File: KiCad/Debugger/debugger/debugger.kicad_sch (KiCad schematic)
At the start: 5 parts, among them J1 Conn_02x16_Odd_Even, J2 Conn_02x16_Odd_Even, J3 CPU Signals, J4 Conn_02x18_Odd_Even

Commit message: debugger wip
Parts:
- removed J1, J2: Conn_02x16_Odd_Even, Connector_PinHeader_2.54mm:PinHeader_2x16_P2.54mm_Vertical, symbol Connector_Generic:Conn_02x16_Odd_Even
- removed J3: CPU Signals, Connector_PinHeader_2.54mm:PinHeader_2x06_P2.54mm_Vertical, symbol 6502-computer-cache:Connector_Generic_Conn_02x06_Odd_Even
- added J10, J19, J7, J8, J9: Conn_01x08, Connector_PinSocket_2.54mm:PinSocket_1x08_P2.54mm_Vertical, symbol Connector_Generic:Conn_01x08
- added J11, J12, J13, J14, J18, J20, J3, J4, J5, J6: Conn_01x08, Connector_PinHeader_2.54mm:PinHeader_1x08_P2.54mm_Vertical, symbol Connector_Generic:Conn_01x08
- added J15, J17: Conn_01x10, Connector_PinHeader_2.54mm:PinHeader_1x10_P2.54mm_Vertical, symbol Connector_Generic:Conn_01x10
- added J16: Conn_01x10, Connector_PinSocket_2.54mm:PinSocket_1x10_P2.54mm_Vertical, symbol Connector_Generic:Conn_01x10
- added J2: Conn_02x20_Odd_Even, Connector_IDC:IDC-Header_2x20_P2.54mm_Vertical, symbol Connector_Generic:Conn_02x20_Odd_Even
- added J21: Conn_02x18_Odd_Even, Connector_PinHeader_2.54mm:PinHeader_2x18_P2.54mm_Vertical, symbol Connector_Generic:Conn_02x18_Odd_Even
- renumbered J4 to J1
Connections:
- net GND: now also J2.34 (Pin_34), J2.35 (Pin_35), J21.35 (Pin_35), J21.36 (Pin_36)
- net RDY: now also J1.4 (Pin_4), XA1.D23, J2.2 (Pin_2), J21.4 (Pin_4); no longer J1.3 (Pin_3)
- net R~{W}: now also J1.7 (Pin_7), XA1.D28, J2.7 (Pin_7), J21.7 (Pin_7); no longer J1.8 (Pin_8)
- net SYNC: now also J1.10 (Pin_10), XA1.D29, J2.8 (Pin_8), J21.10 (Pin_10); no longer J1.9 (Pin_9)
- net a0: now also J1.12 (Pin_12), XA1.D31, J2.10 (Pin_10), J21.12 (Pin_12); no longer J1.11 (Pin_11)
- net a1: now also J1.14 (Pin_14), XA1.D33, J2.12 (Pin_12), J21.14 (Pin_14); no longer J1.13 (Pin_13)
- net a10: now also J1.32 (Pin_32), XA1.D51 (D51_MOSI), J2.30 (Pin_30), J21.32 (Pin_32); no longer J1.31 (Pin_31)
- net a11: now also J1.34 (Pin_34), XA1.D53 (D53_CS), J2.32 (Pin_32), J21.34 (Pin_34); no longer J1.33 (Pin_33)
- net a12: now also J1.33 (Pin_33), XA1.D52 (D52_SCK), J2.33 (Pin_33), J21.33 (Pin_33); no longer J1.34 (Pin_34)
- net a13: now also J1.31 (Pin_31), XA1.D50 (D50_MISO), J2.31 (Pin_31), J21.31 (Pin_31); no longer J1.32 (Pin_32)
- net a14: now also J1.29 (Pin_29), XA1.D48, J2.29 (Pin_29), J21.29 (Pin_29); no longer J1.30 (Pin_30)
- net a15: now also J1.27 (Pin_27), XA1.D46, J2.27 (Pin_27), J21.27 (Pin_27); no longer J1.28 (Pin_28)
- net a2: now also J1.16 (Pin_16), XA1.D35, J2.14 (Pin_14), J21.16 (Pin_16); no longer J1.15 (Pin_15)
- net a3: now also J1.18 (Pin_18), XA1.D37, J2.16 (Pin_16), J21.18 (Pin_18); no longer J1.17 (Pin_17)
- net a4: now also J1.20 (Pin_20), XA1.D39, J2.18 (Pin_18), J21.20 (Pin_20); no longer J1.19 (Pin_19)
- net a5: now also J1.22 (Pin_22), XA1.D41, J2.20 (Pin_20), J21.22 (Pin_22); no longer J1.21 (Pin_21)
- net a6: now also J1.24 (Pin_24), XA1.D43, J2.22 (Pin_22), J21.24 (Pin_24); no longer J1.23 (Pin_23)
- net a7: now also J1.26 (Pin_26), XA1.D45, J2.24 (Pin_24), J21.26 (Pin_26); no longer J1.25 (Pin_25)
- net a8: now also J1.28 (Pin_28), XA1.D47, J2.26 (Pin_26), J21.28 (Pin_28); no longer J1.27 (Pin_27)
- net a9: now also J1.30 (Pin_30), XA1.D49, J2.28 (Pin_28), J21.30 (Pin_30); no longer J1.29 (Pin_29)
- net d0: now also J1.11 (Pin_11), XA1.D30, J2.11 (Pin_11), J21.11 (Pin_11); no longer J1.12 (Pin_12)
- net d1: now also J1.13 (Pin_13), XA1.D32, J2.13 (Pin_13), J21.13 (Pin_13); no longer J1.14 (Pin_14)
- net d2: now also J1.15 (Pin_15), XA1.D34, J2.15 (Pin_15), J21.15 (Pin_15); no longer J1.16 (Pin_16)
- net d3: now also J1.17 (Pin_17), XA1.D36, J2.17 (Pin_17), J21.17 (Pin_17); no longer J1.18 (Pin_18)
- net d4: now also J1.19 (Pin_19), XA1.D38, J2.19 (Pin_19), J21.19 (Pin_19); no longer J1.20 (Pin_20)
- net d5: now also J1.21 (Pin_21), XA1.D40, J2.21 (Pin_21), J21.21 (Pin_21); no longer J1.22 (Pin_22)
- net d6: now also J1.23 (Pin_23), XA1.D42, J2.23 (Pin_23), J21.23 (Pin_23); no longer J1.24 (Pin_24)
- net d7: now also J1.25 (Pin_25), XA1.D44, J2.25 (Pin_25), J21.25 (Pin_25); no longer J1.26 (Pin_26)
- net ~{BE}: now also J1.5 (Pin_5), XA1.D26, J2.5 (Pin_5), J21.5 (Pin_5); no longer J1.6 (Pin_6)
- net ~{IRQ}: now also J1.6 (Pin_6), XA1.D25, J2.4 (Pin_4), J21.6 (Pin_6); no longer J1.5 (Pin_5)
- net ~{NMI}: now also J1.8 (Pin_8), XA1.D27, J2.6 (Pin_6), J21.8 (Pin_8); no longer J1.7 (Pin_7)
- net ~{RES}: now also J1.1 (Pin_1), XA1.D22, J2.1 (Pin_1), J21.1 (Pin_1); no longer J1.2 (Pin_2)
- net ~{SO}: now also J1.3 (Pin_3), XA1.D24, J2.3 (Pin_3), J21.3 (Pin_3); no longer J1.4 (Pin_4)
- net at XA1.3V3 (3.3V): now also J18.5 (Pin_5), J19.5 (Pin_5), J20.4 (Pin_4)
- net at XA1.5V1 (5V): now also J18.4 (Pin_4), J19.4 (Pin_4), J20.5 (Pin_5)
- net at XA1.A0: now also J11.1 (Pin_1), J3.1 (Pin_1), J7.1 (Pin_1)
- net at XA1.A1: now also J11.2 (Pin_2), J3.2 (Pin_2), J7.2 (Pin_2)
- net at XA1.A10: now also J14.6 (Pin_6), J4.3 (Pin_3), J9.6 (Pin_6)
- net at XA1.A11: now also J14.5 (Pin_5), J4.4 (Pin_4), J9.5 (Pin_5)
- net at XA1.A12: now also J14.4 (Pin_4), J4.5 (Pin_5), J9.4 (Pin_4)
- net at XA1.A13: now also J14.3 (Pin_3), J4.6 (Pin_6), J9.3 (Pin_3)
- net at XA1.A14: now also J14.2 (Pin_2), J4.7 (Pin_7), J9.2 (Pin_2)
- net at XA1.A15: now also J14.1 (Pin_1), J4.8 (Pin_8), J9.1 (Pin_1)
- net at XA1.A2: now also J11.3 (Pin_3), J3.3 (Pin_3), J7.3 (Pin_3)
- net at XA1.A3: now also J11.4 (Pin_4), J3.4 (Pin_4), J7.4 (Pin_4)
- net at XA1.A4: now also J11.5 (Pin_5), J3.5 (Pin_5), J7.5 (Pin_5)
- net at XA1.A5: now also J11.6 (Pin_6), J3.6 (Pin_6), J7.6 (Pin_6)
- net at XA1.A6: now also J11.7 (Pin_7), J3.7 (Pin_7), J7.7 (Pin_7)
- net at XA1.A7: now also J11.8 (Pin_8), J3.8 (Pin_8), J7.8 (Pin_8)
- net at XA1.A8: now also J14.8 (Pin_8), J4.1 (Pin_1), J9.8 (Pin_8)
- net at XA1.A9: now also J14.7 (Pin_7), J4.2 (Pin_2), J9.7 (Pin_7)
- net at XA1.AREF: now also J15.8 (Pin_8), J16.8 (Pin_8), J17.8 (Pin_8)
- net at XA1.D0 (D0/RX0): now also J10.1 (Pin_1), J13.1 (Pin_1), J5.1 (Pin_1)
- net at XA1.D1 (D1/TX0): now also J10.2 (Pin_2), J13.2 (Pin_2), J5.2 (Pin_2)
- net at XA1.D10: now also J15.3 (Pin_3), J16.3 (Pin_3), J17.3 (Pin_3)
- net at XA1.D11: now also J15.4 (Pin_4), J16.4 (Pin_4), J17.4 (Pin_4)
- net at XA1.D12: now also J15.5 (Pin_5), J16.5 (Pin_5), J17.5 (Pin_5)
- net at XA1.D13: now also J15.6 (Pin_6), J16.6 (Pin_6), J17.6 (Pin_6)
- net at XA1.D14 (D14/TX3): now also J12.1 (Pin_1), J6.1 (Pin_1), J8.1 (Pin_1)
- net at XA1.D15 (D15/RX3): now also J12.2 (Pin_2), J6.2 (Pin_2), J8.2 (Pin_2)
- net at XA1.D16 (D16/TX2): now also J12.3 (Pin_3), J6.3 (Pin_3), J8.3 (Pin_3)
- net at XA1.D17 (D17/RX2): now also J12.4 (Pin_4), J6.4 (Pin_4), J8.4 (Pin_4)
- net at XA1.D18 (D18/TX1): now also J12.5 (Pin_5), J6.5 (Pin_5), J8.5 (Pin_5)
- net at XA1.D19 (D19/RX1): now also J12.6 (Pin_6), J6.6 (Pin_6), J8.6 (Pin_6)
- net at XA1.D2 (D2_INT0): now also J10.3 (Pin_3), J13.3 (Pin_3), J5.3 (Pin_3)
- net at XA1.D20 (D20/SDA): now also J12.7 (Pin_7), J6.7 (Pin_7), J8.7 (Pin_7)
- net at XA1.D21 (D21/SCL): now also J12.8 (Pin_8), J6.8 (Pin_8), J8.8 (Pin_8)
- net at XA1.D3 (D3_INT1): now also J10.4 (Pin_4), J13.4 (Pin_4), J5.4 (Pin_4)
- net at XA1.D4: now also J10.5 (Pin_5), J13.5 (Pin_5), J5.5 (Pin_5)
- net at XA1.D5: now also J10.6 (Pin_6), J13.6 (Pin_6), J5.6 (Pin_6)
- net at XA1.D6: now also J10.7 (Pin_7), J13.7 (Pin_7), J5.7 (Pin_7)
- net at XA1.D7: now also J10.8 (Pin_8), J13.8 (Pin_8), J5.8 (Pin_8)
- net at XA1.D8: now also J15.1 (Pin_1), J16.1 (Pin_1), J17.1 (Pin_1)
- net at XA1.D9: now also J15.2 (Pin_2), J16.2 (Pin_2), J17.2 (Pin_2)
- net at XA1.GND1 (GND): now also J15.7 (Pin_7), J16.7 (Pin_7), J17.7 (Pin_7)
- net at XA1.GND2 (GND): now also J18.3 (Pin_3), J19.3 (Pin_3), J20.6 (Pin_6)
- net at XA1.GND3 (GND): now also J18.2 (Pin_2), J19.2 (Pin_2), J20.7 (Pin_7)
- net at XA1.IORF (IOREF): now also J18.7 (Pin_7), J19.7 (Pin_7), J20.2 (Pin_2)
- net at XA1.RST1 (RESET): now also J18.6 (Pin_6), J19.6 (Pin_6), J20.3 (Pin_3)
- net at XA1.SCL: now also J15.10 (Pin_10), J16.10 (Pin_10), J17.10 (Pin_10)
- net at XA1.SDA: now also J15.9 (Pin_9), J16.9 (Pin_9), J17.9 (Pin_9)
- net at XA1.VIN: now also J18.1 (Pin_1), J19.1 (Pin_1), J20.8 (Pin_8)
- new net: J18.8 (Pin_8), J19.8 (Pin_8), J20.1 (Pin_1)
- no-connect marks 2 -> 7
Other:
- note removed: "Added header for the additional signals CPU and ROM"
- moved on the sheet: J1

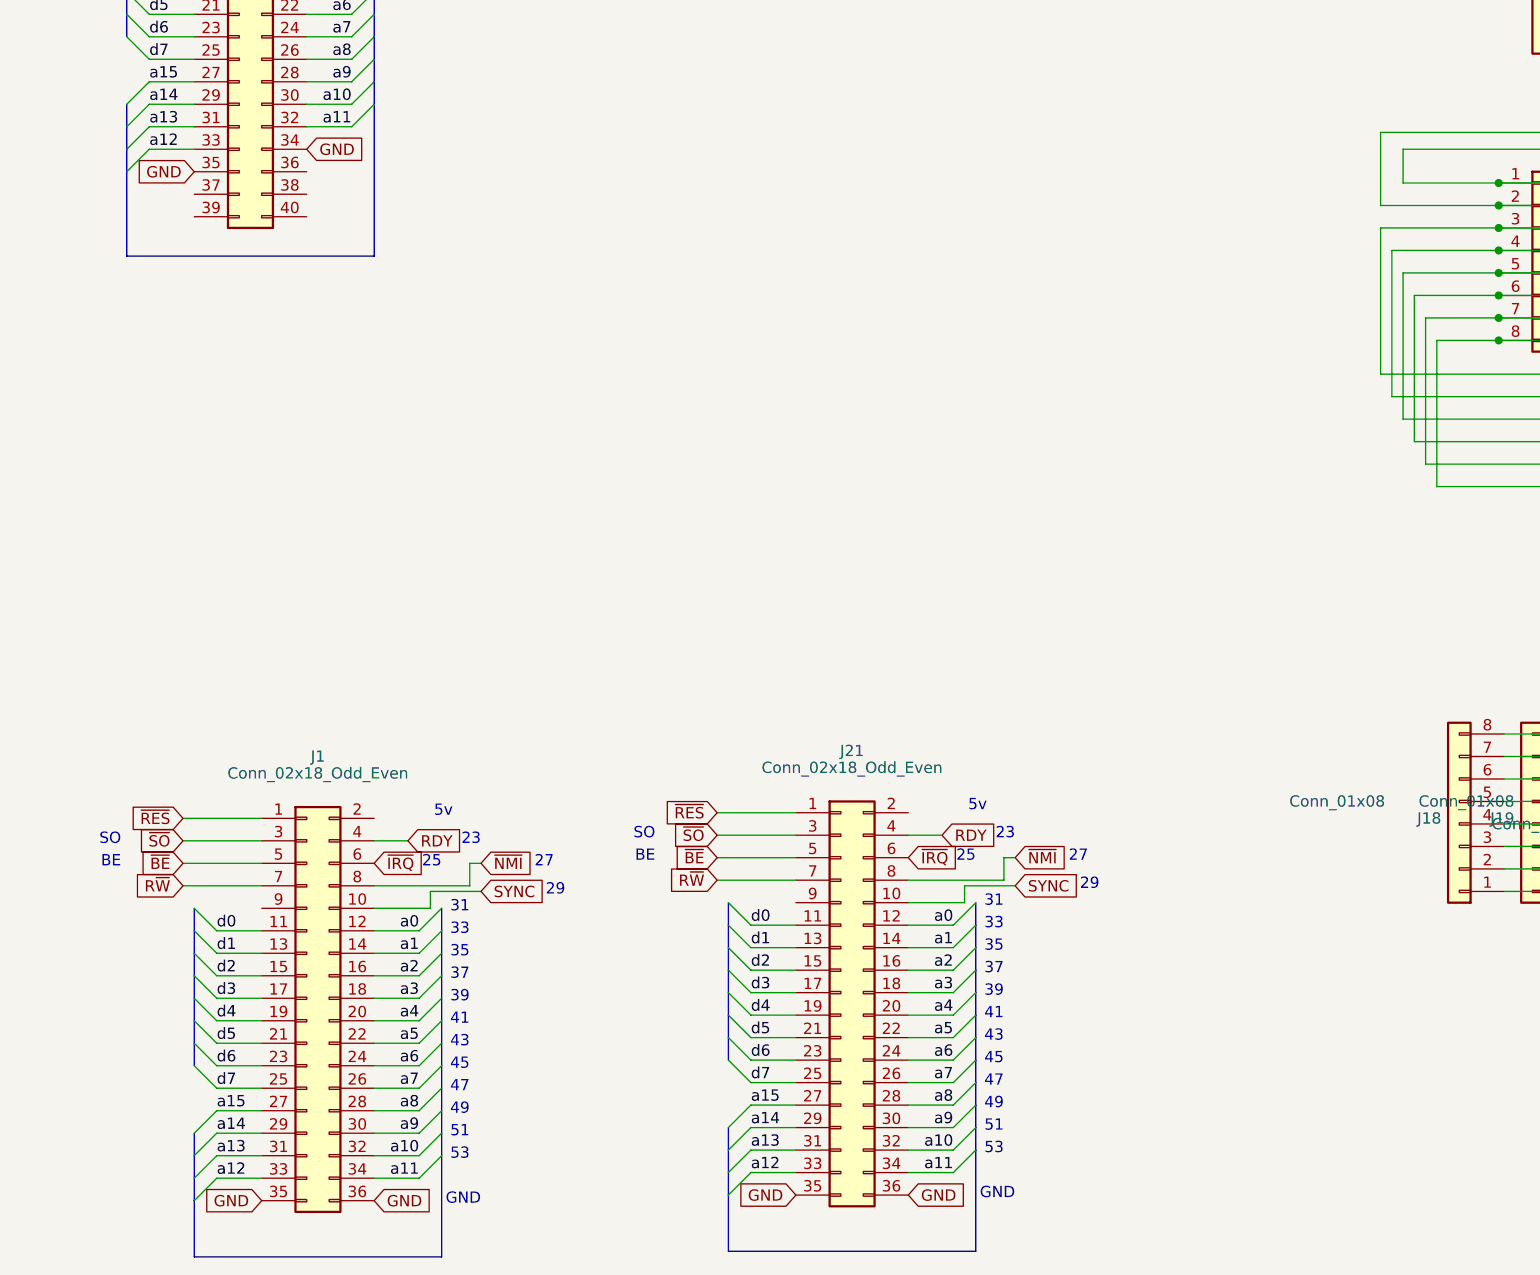
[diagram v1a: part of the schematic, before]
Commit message: Silkscreen Updates
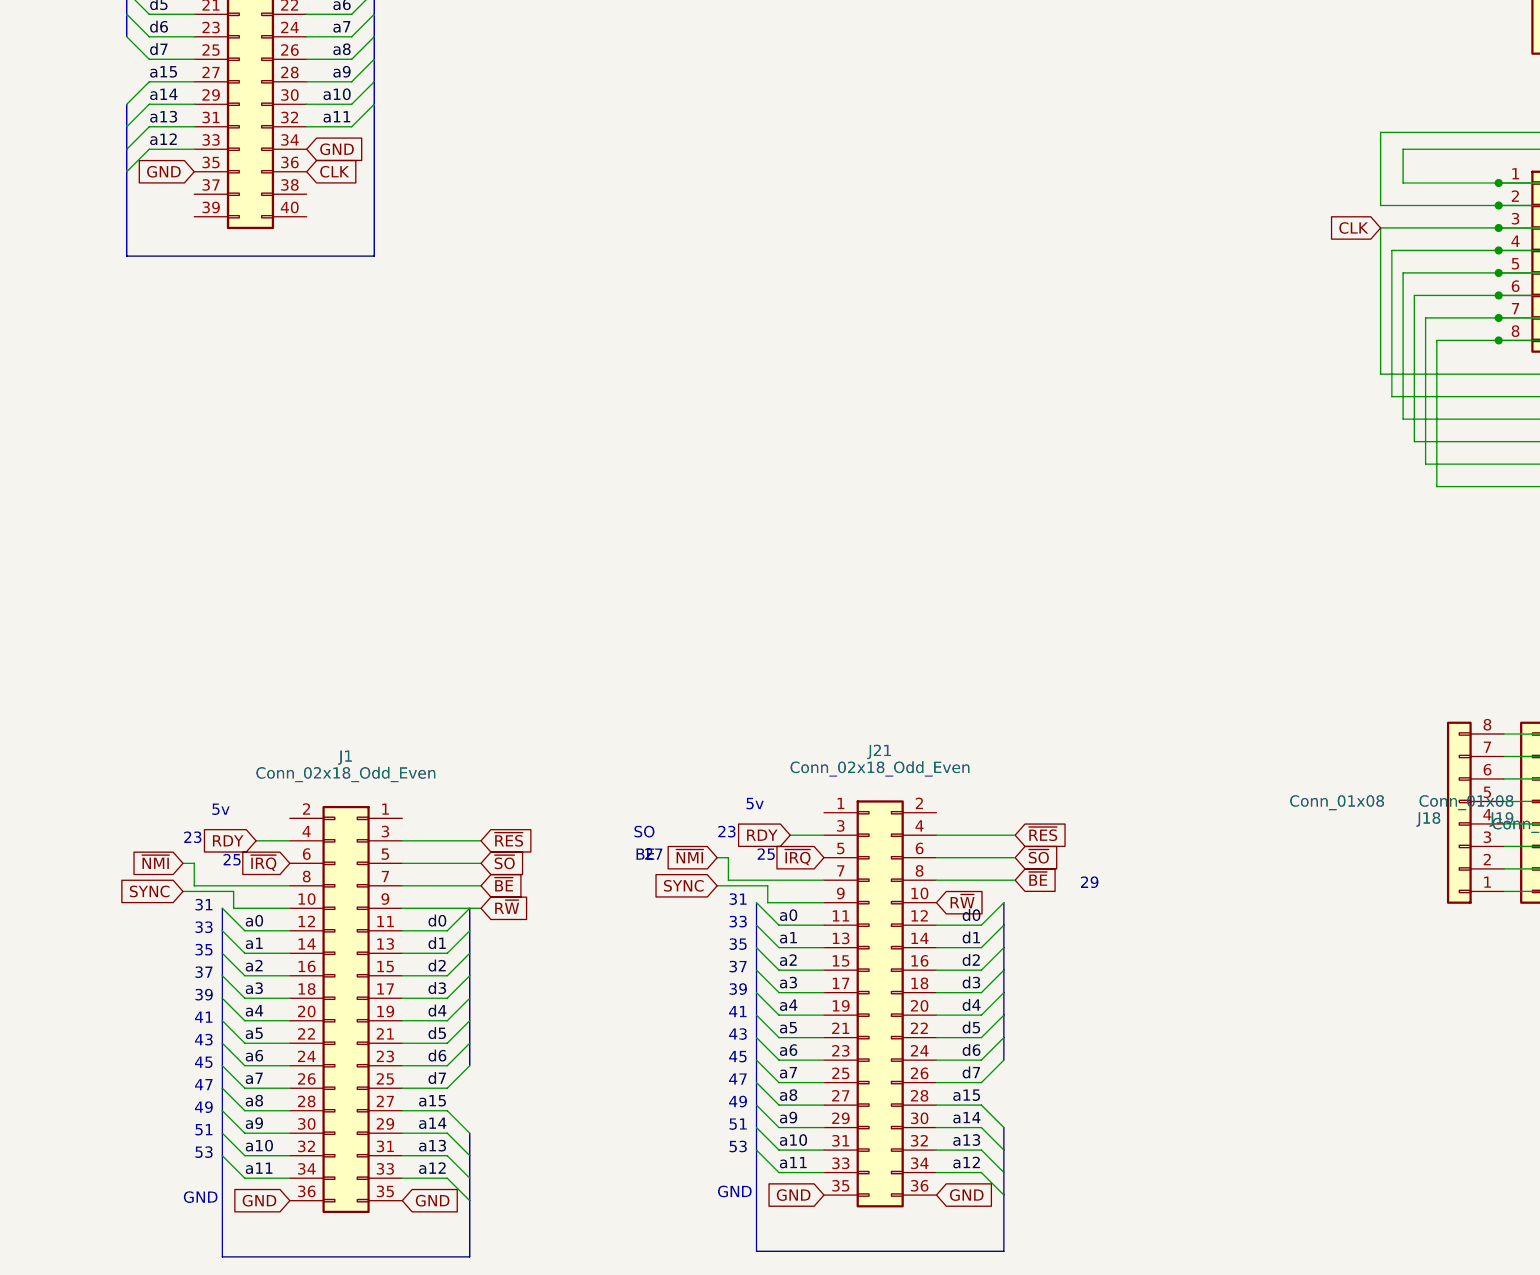
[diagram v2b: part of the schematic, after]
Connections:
- net RDY: now also J21.3 (Pin_3); no longer J21.4 (Pin_4)
- net R~{W}: now also J1.9 (Pin_9), J21.10 (Pin_10); no longer J1.7 (Pin_7), J21.7 (Pin_7)
- net SYNC: now also J21.9 (Pin_9); no longer J21.10 (Pin_10)
- net a0: now also J21.11 (Pin_11); no longer J21.12 (Pin_12)
- net a1: now also J21.13 (Pin_13); no longer J21.14 (Pin_14)
- net a10: now also J21.31 (Pin_31); no longer J21.32 (Pin_32)
- net a11: now also J21.33 (Pin_33); no longer J21.34 (Pin_34)
- net a12: now also J21.34 (Pin_34); no longer J21.33 (Pin_33)
- net a13: now also J21.32 (Pin_32); no longer J21.31 (Pin_31)
- net a14: now also J21.30 (Pin_30); no longer J21.29 (Pin_29)
- net a15: now also J21.28 (Pin_28); no longer J21.27 (Pin_27)
- net a2: now also J21.15 (Pin_15); no longer J21.16 (Pin_16)
- net a3: now also J21.17 (Pin_17); no longer J21.18 (Pin_18)
- net a4: now also J21.19 (Pin_19); no longer J21.20 (Pin_20)
- net a5: now also J21.21 (Pin_21); no longer J21.22 (Pin_22)
- net a6: now also J21.23 (Pin_23); no longer J21.24 (Pin_24)
- net a7: now also J21.25 (Pin_25); no longer J21.26 (Pin_26)
- net a8: now also J21.27 (Pin_27); no longer J21.28 (Pin_28)
- net a9: now also J21.29 (Pin_29); no longer J21.30 (Pin_30)
- net d0: now also J21.12 (Pin_12); no longer J21.11 (Pin_11)
- net d1: now also J21.14 (Pin_14); no longer J21.13 (Pin_13)
- net d2: now also J21.16 (Pin_16); no longer J21.15 (Pin_15)
- net d3: now also J21.18 (Pin_18); no longer J21.17 (Pin_17)
- net d4: now also J21.20 (Pin_20); no longer J21.19 (Pin_19)
- net d5: now also J21.22 (Pin_22); no longer J21.21 (Pin_21)
- net d6: now also J21.24 (Pin_24); no longer J21.23 (Pin_23)
- net d7: now also J21.26 (Pin_26); no longer J21.25 (Pin_25)
- net ~{BE}: now also J1.7 (Pin_7), J21.8 (Pin_8); no longer J1.5 (Pin_5), J21.5 (Pin_5)
- net ~{IRQ}: now also J21.5 (Pin_5); no longer J21.6 (Pin_6)
- net ~{NMI}: now also J21.7 (Pin_7); no longer J21.8 (Pin_8)
- net ~{RES}: now also J1.3 (Pin_3), J21.4 (Pin_4); no longer J1.1 (Pin_1), J21.1 (Pin_1)
- net ~{SO}: now also J1.5 (Pin_5), J21.6 (Pin_6); no longer J1.3 (Pin_3), J21.3 (Pin_3)
- net CLK: now reaches J2.36 (Pin_36)
- net CLK: now also J11.3 (Pin_3), J3.3 (Pin_3), J7.3 (Pin_3), XA1.A2
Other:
- moved on the sheet: J1, J21
